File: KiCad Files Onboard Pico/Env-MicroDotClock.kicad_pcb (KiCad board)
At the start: 2 copper layers, 110 x 80 mm, 101 parts, among them IC1 IS31FL3730-QFLS2-TR, IC2 IS31FL3730-QFLS2-TR, IC3 IS31FL3730-QFLS2-TR, IC4 IS31FL3730-QFLS2-TR, J1 1mm 1x3, J2 GT-USB-7051A, J3 Button, J4 TYPE-C-31-M-12, M1 Dip-14 Socket, M2 Dip-14 Socket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

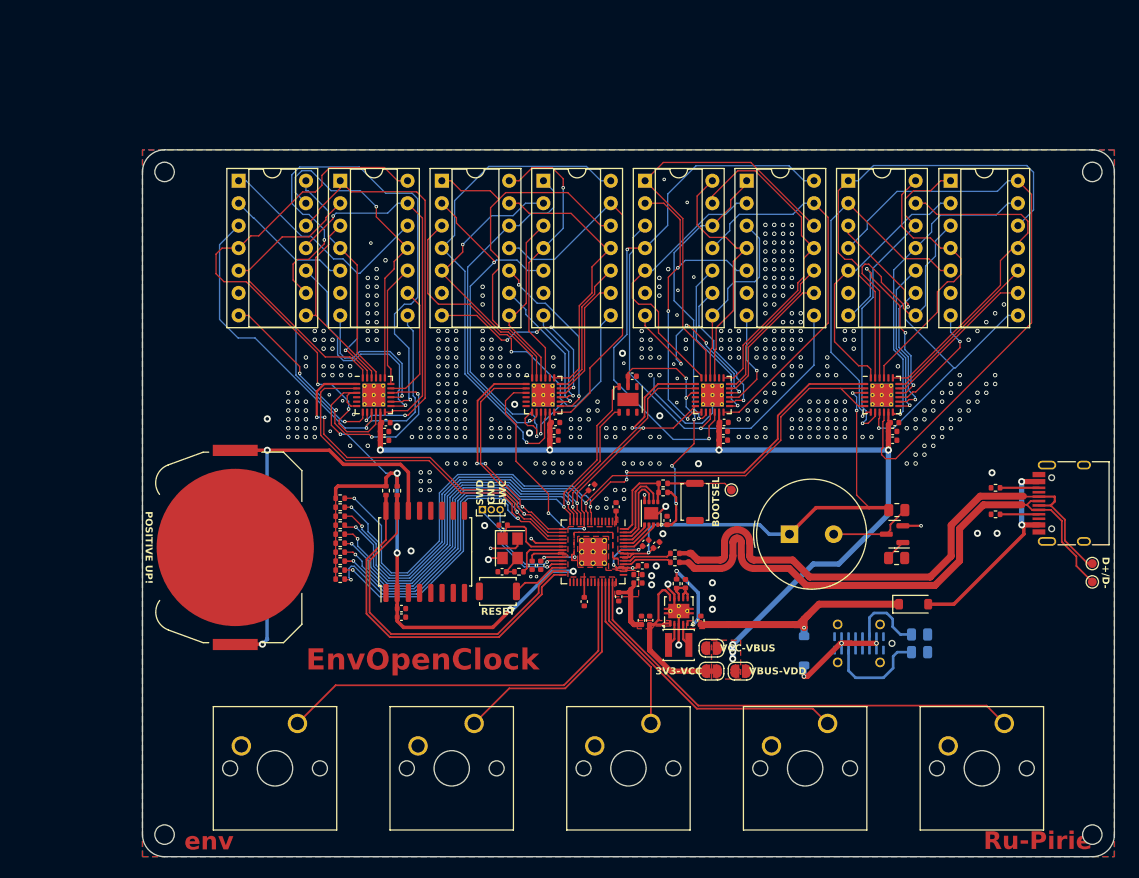
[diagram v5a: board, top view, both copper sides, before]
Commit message: Moved all ICs to one i2c bus, removed SI7021, added i2c level shifters.
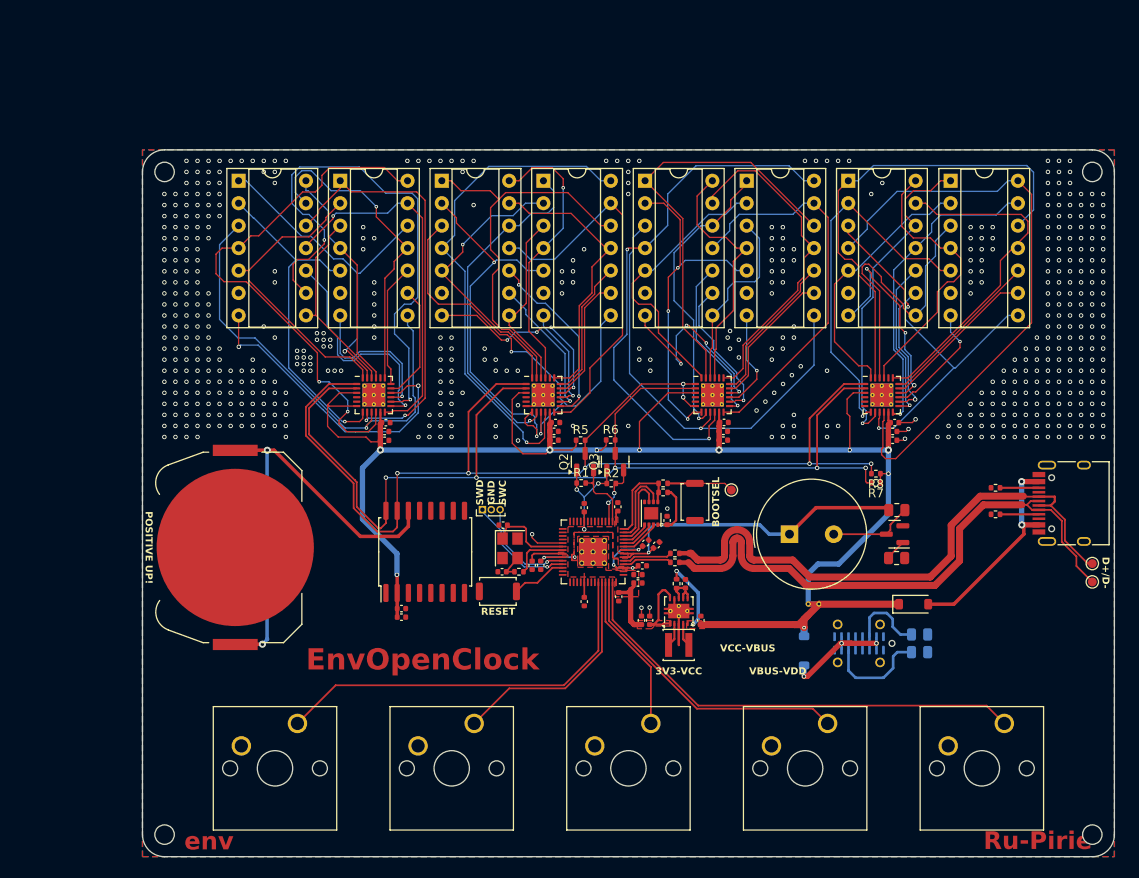
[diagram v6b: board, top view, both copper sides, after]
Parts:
- removed C33: 0402 0.1uF, Capacitor_SMD:C_0402_1005Metric
- removed JP1: bridge, Jumper:SolderJumper-2_P1.3mm_Bridged_RoundedPad1.0x1.5mm
- removed JP2, JP3: bridge, Jumper:SolderJumper-2_P1.3mm_Open_RoundedPad1.0x1.5mm
- removed R10, R11, R12, R13, R28, R9: 0402 10K, Resistor_SMD:R_0402_1005Metric
- removed U1: Si7021-A20, Package_DFN_QFN:DFN-6-1EP_3x3mm_P1mm_EP1.5x2.4mm
- added NT3: NetTie_2, NetTie:NetTie-2_THT_Pad0.3mm, F.Cu at (88.8, 64.9)
- added Q2: BSS138, Package_TO_SOT_SMD:SOT-23, F.Cu at (63.6, 48.8)
- added Q3: BSS138, Package_TO_SOT_SMD:SOT-23, F.Cu at (67.0, 48.8)
- R1, R2, R5, R6, R7, R8: value 0402 10K -> 10K 0402
- moved R8 60.9 mm to (96.5, 50.1), turned to 180 degrees
- moved R7 60.8 mm to (96.5, 51.2), turned to 180 degrees
- moved R6 31.5 mm to (66.5, 46.3)
- moved R5 28.0 mm to (63.1, 46.4)
- moved R2 24.2 mm to (66.6, 51.3), turned to 0 degrees
- moved R1 22.1 mm to (63.1, 51.2), turned to 0 degrees
- moved C30 2.44 mm to (63.5, 54.0), turned to 90 degrees
- moved C31 0.20 mm to (67.3, 53.9)
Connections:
- C10 pad 1: +3V3 -> VCC
- C9 pad 1: +3V3 -> VCC
- IC1 pad 1: GPIO14 -> i2c-sda
- IC1 pad 2: GPIO15 -> i2c-scl
- IC1 pad 3: +3V3 -> VCC
- IC1 pad 6: +3V3 -> VCC
- IC2 pad 1: GPIO12 -> i2c-sda
- IC2 pad 2: GPIO13 -> i2c-scl
- IC2 pad 3: +3V3 -> VCC
- IC3 pad 1: GPIO8 -> i2c-sda
- IC3 pad 2: GPIO9 -> i2c-scl
- IC3 pad 3: +3V3 -> VCC
- IC3 pad 6: GPIO8 -> i2c-sda
- IC4 pad 1: GPIO6 -> i2c-sda
- IC4 pad 2: GPIO7 -> i2c-scl
- IC4 pad 3: +3V3 -> VCC
- IC4 pad 6: GPIO7 -> i2c-scl
- R1 pad 2: GPIO17 -> 3v3_i2c_sda
- R2 pad 2: GPIO16 -> 3v3_i2c_scl
- R5 pad 1: +3V3 -> VCC
- R5 pad 2: GPIO6 -> i2c-sda
- R6 pad 1: +3V3 -> VCC
- R6 pad 2: GPIO7 -> i2c-scl
- R7 pad 1: +3V3 -> VCC
- R7 pad 2: GPIO8 -> i2c-scl
- R8 pad 1: +3V3 -> VCC
- R8 pad 2: GPIO9 -> i2c-sda
- U3 pad 15: GPIO16 -> i2c-sda
- U3 pad 16: GPIO17 -> i2c-scl
- U3 pad 2: +3V3 -> VCC
- U4 pad 2: GPIO0 -> 3v3_i2c_sda
- U4 pad 3: GPIO1 -> 3v3_i2c_scl
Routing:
- net +3V3: track 224.2 -> 80.4 mm, vias 16 -> 5
- net i2c-sda: track 0.00 -> 137.4 mm, vias 0 -> 7
- net i2c-scl: track 0.00 -> 129.4 mm, vias 0 -> 5
- net GPIO7: track 85.7 -> 0.00 mm, vias 2 -> 0
- net GPIO6: track 84.5 -> 0.00 mm, vias 4 -> 0
- net GPIO14: track 74.1 -> 0.00 mm, vias 4 -> 0
- net GPIO8: track 72.4 -> 0.00 mm, vias 4 -> 0
- net GPIO15: track 71.9 -> 0.00 mm, vias 2 -> 0
- net VCC: track 108.2 -> 174.5 mm, vias 7 -> 9
- net GPIO9: track 62.6 -> 0.00 mm, vias 2 -> 0
- net GPIO12: track 57.3 -> 0.00 mm, vias 4 -> 0
- net GPIO13: track 56.4 -> 0.00 mm, vias 2 -> 0
- net GPIO11: track 54.4 -> 0.00 mm, vias 2 -> 0
- net GPIO10: track 52.6 -> 0.00 mm, vias 2 -> 0
- net GPIO17: track 41.0 -> 0.00 mm
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- removed copper zone on F.Cu, net VCC

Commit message: Fixed issues with I2C, added I2C shifter
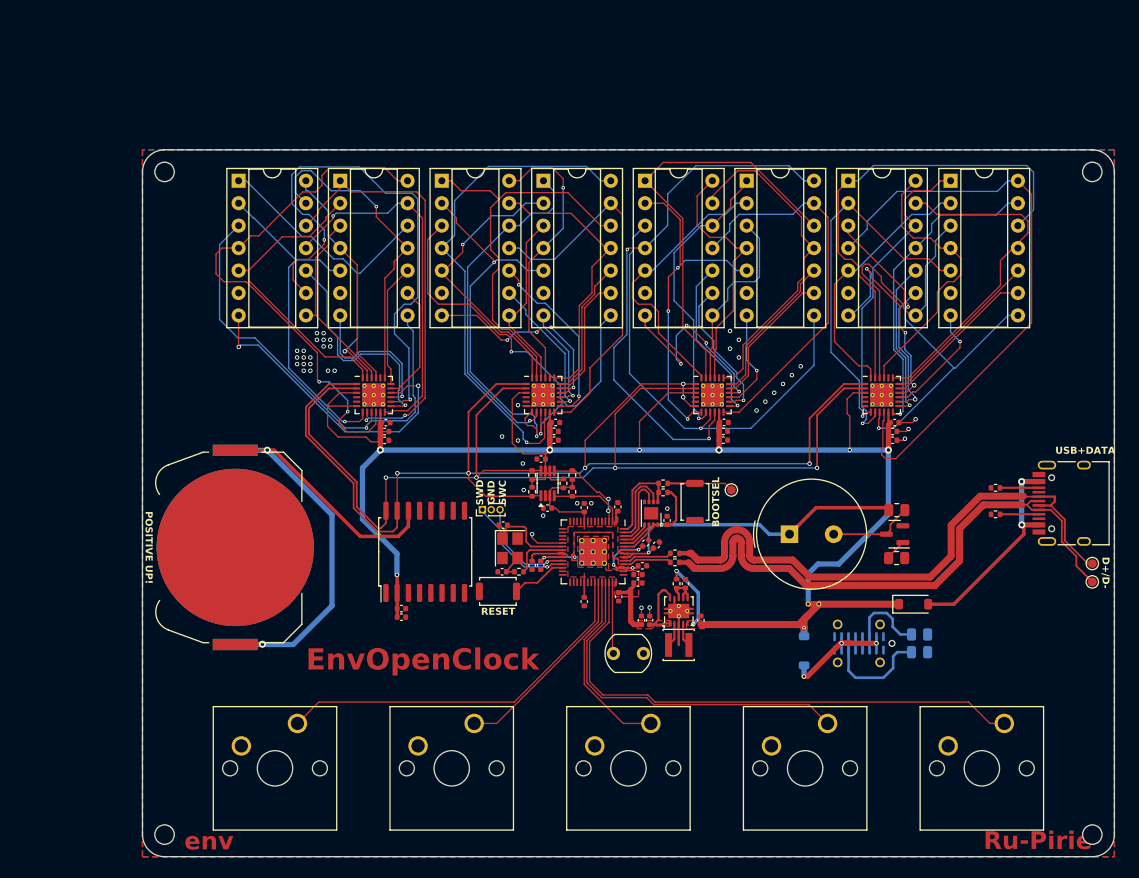
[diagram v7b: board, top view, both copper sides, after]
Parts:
- removed Q2, Q3: BSS138, Package_TO_SOT_SMD:SOT-23
- removed R8: 10K 0402, Resistor_SMD:R_0402_1005Metric
- added BT1: Keystone 3034, Battery:BatteryHolder_Keystone_3034_1x20mm, B.Cu at (24.0, 58.5)
- added C33: 0.1uF 0402, Capacitor_SMD:C_0402_1005Metric, F.Cu at (59.4, 54.0)
- added C34: 0.1uF 0402, Capacitor_SMD:C_0402_1005Metric, F.Cu at (58.6, 48.5)
- added R9: 10kΩ 20kΩ 3.4mm, OptoDevice:R_LDR_5.1x4.3mm_P3.4mm_Vertical, F.Cu at (66.8, 70.5)
- added U1: TCA9406DC, Package_SO:VSSOP-8_2.3x2mm_P0.5mm, F.Cu at (59.4, 51.2)
- moved R7 38.9 mm to (57.6, 52.2), turned to 90 degrees
- moved R6 9.73 mm to (57.6, 50.3), turned to -90 degrees
- moved R5 5.26 mm to (61.1, 51.2), turned to -90 degrees
- moved R2 4.51 mm to (62.1, 52.2), turned to 90 degrees
- moved R1 1.35 mm to (62.1, 50.3), turned to -90 degrees
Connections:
- R1 pad 1: +3V3 -> 3v3_i2c_scl
- R1 pad 2: 3v3_i2c_sda -> +3V3
- R2 pad 1: +3V3 -> 3v3_i2c_sda
- R2 pad 2: 3v3_i2c_scl -> +3V3
- R5 pad 1: VCC -> Net-(U1-OE)
- R5 pad 2: i2c-sda -> +3V3
- R6 pad 1: VCC -> i2c-scl
- R6 pad 2: i2c-scl -> VCC
- R7 pad 1: VCC -> i2c-sda
- R7 pad 2: i2c-scl -> VCC
- SW1 pad 1: GPIO25 -> GPIO24
- SW2 pad 1: ADC0 -> GPIO25
- SW3 pad 1: ADC1 -> ADC0
- SW4 pad 1: ADC2 -> ADC1
- SW5 pad 1: ADC3 -> ADC2
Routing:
- net ADC3: track 53.5 -> 8.10 mm
- net GPIO24: track 0.00 -> 42.9 mm
- net ADC2: track 33.9 -> 61.1 mm
- net ADC1: track 18.1 -> 41.4 mm
- net GPIO25: track 45.2 -> 23.3 mm
- net Net-(BT1-+): track 51.2 -> 69.1 mm
- net ADC0: track 25.7 -> 21.8 mm
- net 3v3_i2c_scl: track 6.99 -> 10.1 mm
- net Net-(U1-OE): track 0.00 -> 2.51 mm
- net +3V3: track 80.4 -> 78.1 mm, vias 5 -> 2
- net VCC: track 174.5 -> 172.7 mm, vias 9 -> 7
- net i2c-sda: track 137.4 -> 139.0 mm, vias 7 -> 6
- net i2c-scl: track 129.4 -> 129.3 mm, vias 5 -> 4
- net GND: vias 549 -> 44
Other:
- board text added: "EnvOpenDesigns"
- board text added: "USB+DATA"
- board text removed: "3V3-VCC"
- board text removed: "VBUS-VDD"
- board text removed: "VCC-VBUS"

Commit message: corrected couple missing connections
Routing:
- net i2c-scl: track 129.3 -> 134.1 mm, vias 4 -> 6
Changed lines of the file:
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@@
 		(tags "capacitor")
 		(property "Reference" "C34"
-			(at 0 -1.16 360)
+			(at 0 -1.16 0)
 			(layer "F.SilkS")
 			(hide yes)
@@
 		)
 		(property "Value" "0.1uF 0402"
-			(at 0 1.16 360)
+			(at 0 1.16 0)
 			(layer "F.Fab")
 			(effects
@@
 		)
 		(fp_text user "${REFERENCE}"
-			(at 0 0 360)
+			(at 0 0 0)
 			(layer "F.Fab")
 			(effects
@@
 		(tags "capacitor")
 		(property "Reference" "C33"
-			(at 0 -1.16 360)
+			(at 0 -1.16 0)
 			(layer "F.SilkS")
 			(hide yes)
@@
 		)
 		(property "Value" "0.1uF 0402"
-			(at 0 1.16 360)
+			(at 0 1.16 0)
 			(layer "F.Fab")
 			(effects
@@
 		)
 		(fp_text user "${REFERENCE}"
-			(at 0 0 360)
+			(at 0 0 0)
 			(layer "F.Fab")
 			(effects
@@
 	)
 	(segment
-		(start 92.894974 40.5)
-		(end 89.85 43.544974)
-		(width 0.2)
+		(start 92.75 41)
+		(end 92.75 40.75)
+		(width 0.15)
 		(layer "F.Cu")
 		(net 149)
@@
 	)
 	(segment
+		(start 92.697487 40.697487)
+		(end 92.572487 40.822487)
+		(width 0.2)
+		(layer "F.Cu")
+		(net 149)
+	)
+	(segment
 		(start 76.0758 40.5)
 		(end 69.886764 40.5)
@@
 	)
 	(segment
+		(start 92.822487 40.572487)
+		(end 92.697487 40.697487)
+		(width 0.2)
+		(layer "F.Cu")
+		(net 149)
+	)
+	(segment
+		(start 92.572487 40.822487)
+		(end 89.85 43.544974)
+		(width 0.2)
+		(layer "F.Cu")
+		(net 149)
+	)
+	(segment
 		(start 56.9142 40.5)
 		(end 54.3 40.5)
@@
 	)
 	(segment
+		(start 92.894974 40.5)
+		(end 92.822487 40.572487)
+		(width 0.2)
+		(layer "F.Cu")
+		(net 149)
+	)
+	(segment
 		(start 37.75 53.905026)
 		(end 37.75 51.105025)
@@
 	)
 	(segment
+		(start 92.75 42.5)
+		(end 92.75 41)
+		(width 0.15)
+		(layer "F.Cu")
+		(net 149)
+	)
+	(segment
 		(start 37.544975 50.9)
 		(end 37.544974 50.9)
@@
 	)
 	(segment
+		(start 92.75 40.75)
+		(end 92.697487 40.697487)
+		(width 0.15)
+		(layer "F.Cu")
+		(net 149)
+	)
+	(segment
 		(start 54.3 40.5)
 		(end 51.3 43.5)
@@
 	)
 	(segment
+		(start 92.75 40.75)
+		(end 92.75 40.644974)
+		(width 0.15)
+		(layer "F.Cu")
+		(net 149)
+	)
+	(segment
+		(start 95.2375 42.5)
+		(end 94.1518 42.5)
+		(width 0.15)
+		(layer "F.Cu")
+		(net 149)
+	)
+	(segment
+		(start 92.572487 40.822487)
+		(end 92.75 41)
+		(width 0.15)
+		(layer "F.Cu")
+		(net 149)
+	)
+	(segment
 		(start 32.35 42.744974)
 		(end 34.594974 40.5)
@@
 	)
 	(segment
+		(start 92.75 40.644974)
+		(end 92.822487 40.572487)
+		(width 0.15)
+		(layer "F.Cu")
+		(net 149)
+	)
+	(segment
 		(start 41.055 55.745)
 		(end 40.45 56.35)
@@
 	)
 	(via
+		(at 92.75 42.5)
+		(size 0.5)
+		(drill 0.3)
+		(layers "F.Cu" "B.Cu")
+		(net 149)
+	)
+	(via
 		(at 41.05 50.6)
 		(size 0.5)
@@
 	)
 	(via
+		(at 94.1518 42.5)
+		(size 0.5)
+		(drill 0.3)
+		(layers "F.Cu" "B.Cu")
+		(net 149)
+	)
+	(via
 		(at 67 49.5)
 		(size 0.5)
@@
 		(width 0.15)
 		(layer "B.Cu")
+		(net 149)
+	)
+	(segment
+		(start 94.1518 42.5)
+		(end 92.75 42.5)
+		(width 0.15)
+		(layer "B.Cu")
